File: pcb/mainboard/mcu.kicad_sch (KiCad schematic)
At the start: 54 parts, among them Y100 24MHz, Y101 32.768K

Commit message: Working on mainboard schematics
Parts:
- removed C137, C138: 18pF, Capacitor_SMD:C_0402_1005Metric, symbol Device:C
- removed Y101: 32.768K, Crystal:Crystal_SMD_TXC_9HT11-2Pin_2.0x1.2mm_HandSoldering, symbol Device:Crystal
- added R?: 100K/1%, Resistor_SMD:R_0402_1005Metric, symbol Device:R
- added R?: 10K, Resistor_SMD:R_0402_1005Metric, symbol Device:R
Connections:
- net GND: now also R?.1, R?.1
- net RTC_0P8: now also U?.B25 (RTC_XTALO)
- net PMIC_ON_REQ: now reaches U?.A24 (PMIC_ON_REQ)
- net CLK_32K_OUT: now reaches U?.A26 (RTC_XTALI)
- net POR_B: now reaches U?.B24 (POR_B)
- net at U?.D27 (JTAG_MOD): now also R?.2
- net PMIC_STBY_REQ: now reaches U?.E24 (PMIC_STBY_REQ)
- net RTC_RESET_B: now reaches U?.F24 (RTC_RESET_B)
- net at U?.J24 (TSENSOR_RES_EXT): now also R?.2
- no-connect marks 12 -> 17
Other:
- moved on the sheet: C123, C124, U?L, Y100

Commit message: Mainboard schematics WIP
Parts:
- gave numbers to parts that had none: 48
- renumbered C123 to C218, C124 to C224, Y100 to Y201

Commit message: Draft motherboard schematics for r0.0 layout
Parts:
- added R203: 100K, Resistor_SMD:R_0402_1005Metric, symbol Device:R
- added R204, R205, R206, R207: 10K, Resistor_SMD:R_0402_1005Metric, symbol Device:R
- added SW201: SW_Push, Button_Switch_SMD:SW_SPST_SKQG_WithStem, symbol Switch:SW_Push
- C202, C203: footprint Capacitor_SMD:C_0402_1005Metric -> Capacitor_SMD:C_0201_0603Metric
- R202: value 100K/1% -> 100K/1%
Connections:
- net GND: now also R204.1, R207.1, SW201.2
- net RTC_1P8: now also R203.2, R205.1, R206.1
- net ONOFF: now reaches U201.A25 (ONOFF)
- net ONOFF: now also R203.1
- net at U201.C27 (BOOT_MODE2): now also R206.2, SW201.1
- net at U201.D26 (BOOT_MODE3): now also R207.2
- net at U201.G26 (BOOT_MODE0): now also R204.2
- net at U201.G27 (BOOT_MODE1): now also R205.2
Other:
- note added: "QSPI boot by default, press button changes to eMMC boot (invalid) so it should fallback to USB"

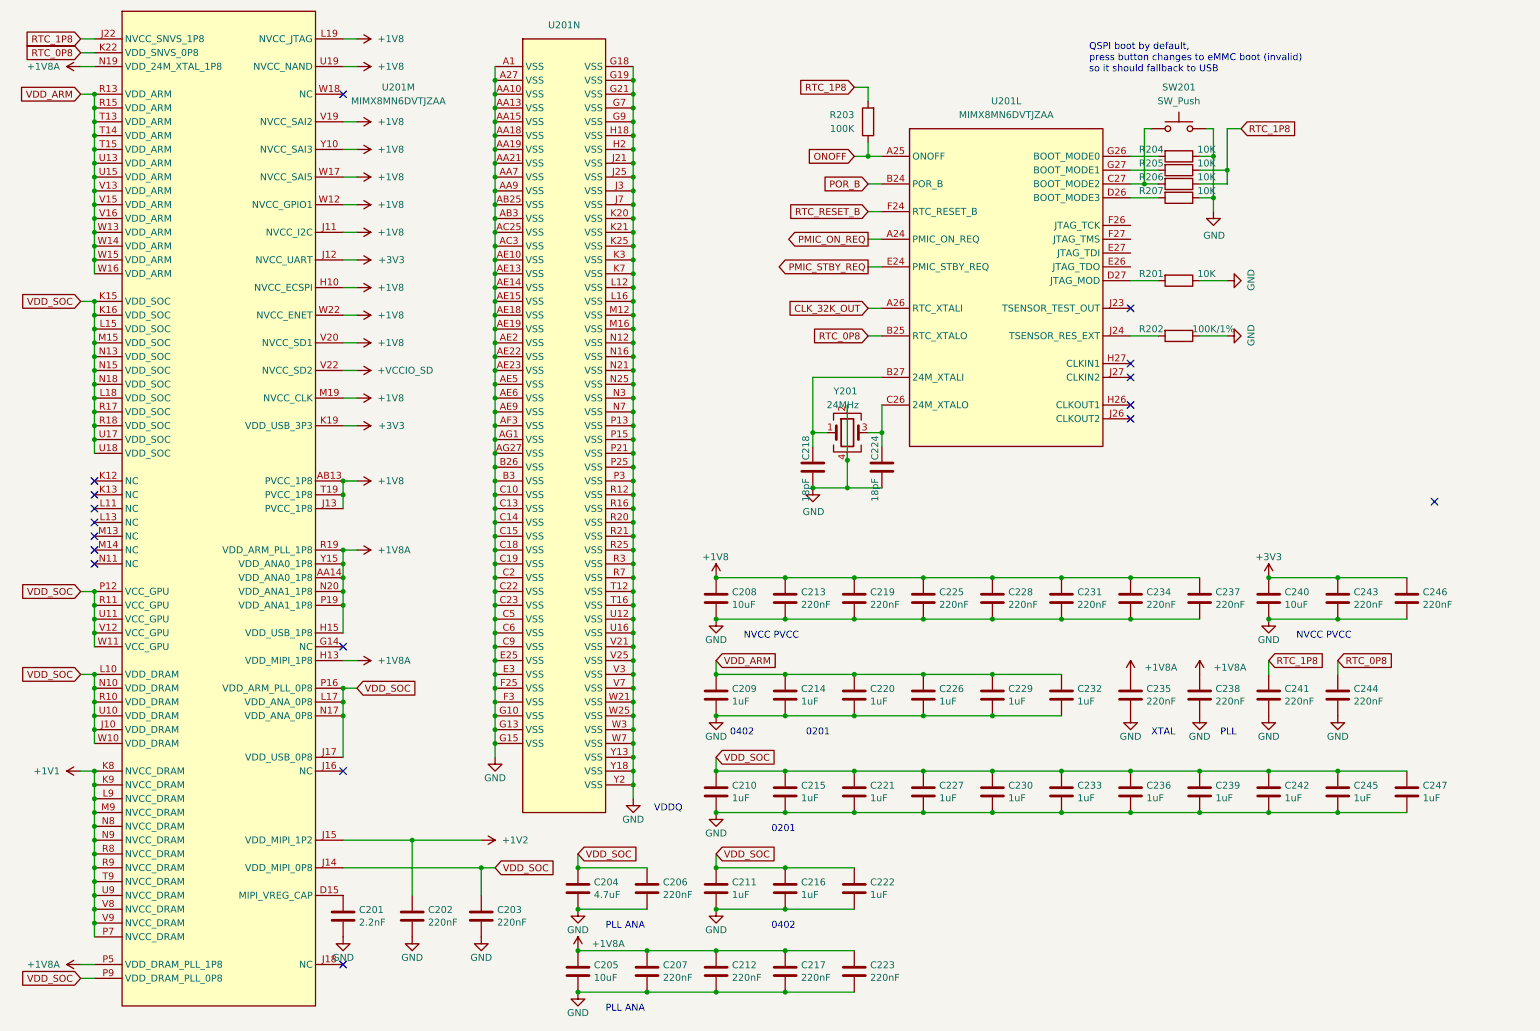
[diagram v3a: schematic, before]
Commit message: Motherboard PCB component initial placement, schematics fixes
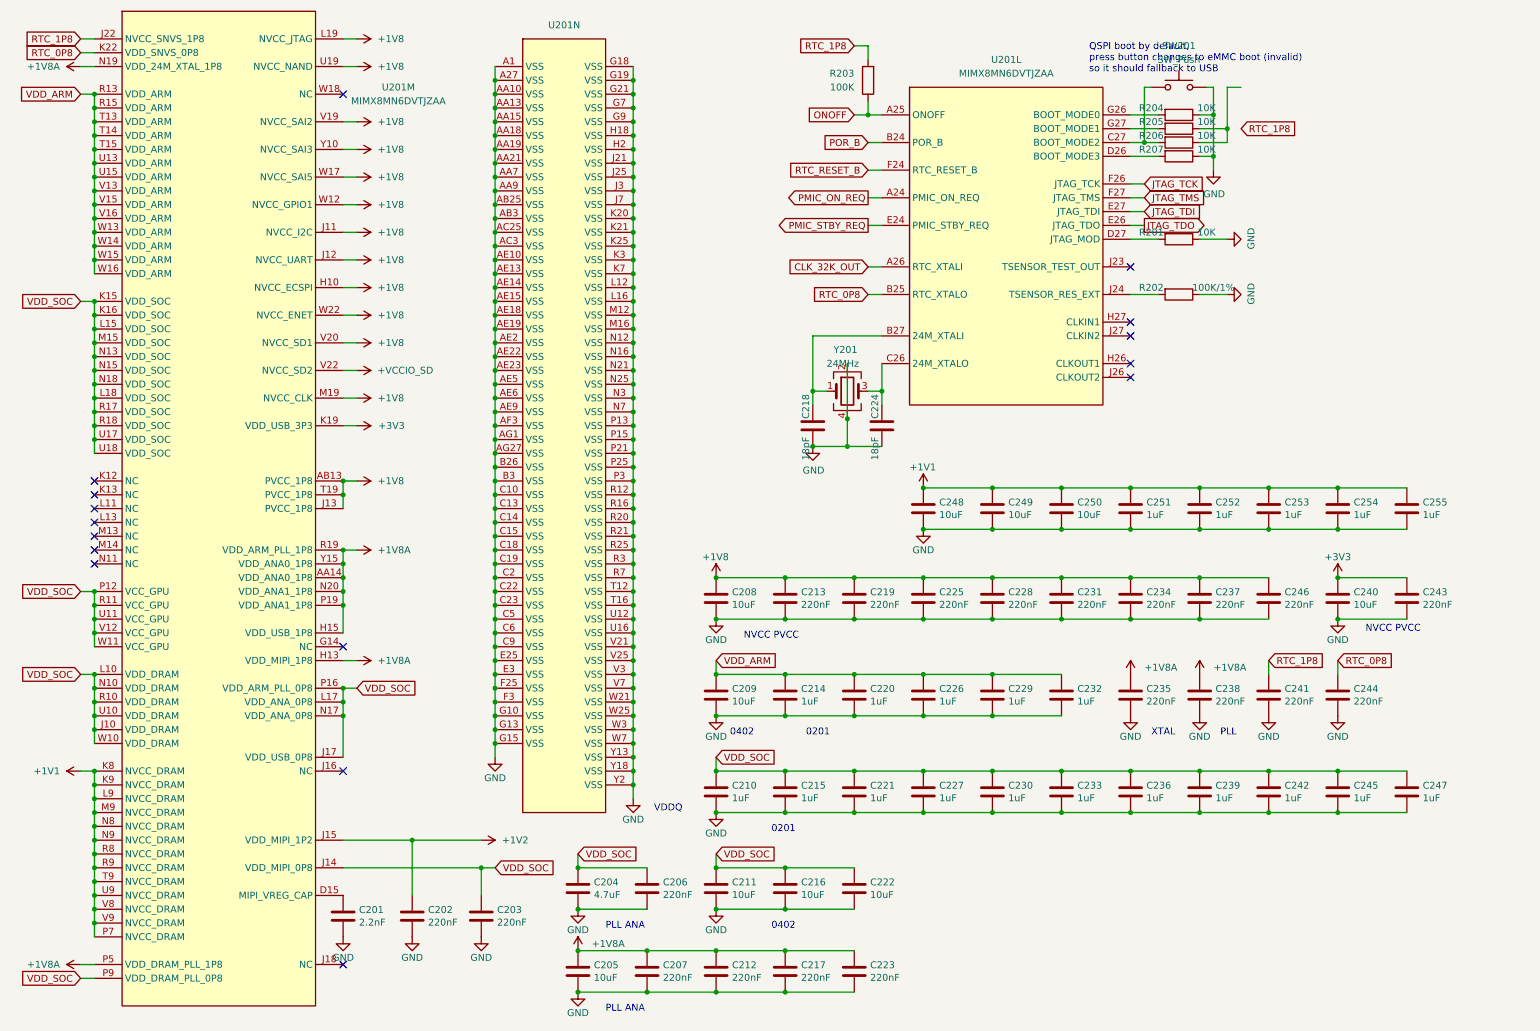
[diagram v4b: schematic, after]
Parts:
- added C248, C249, C250: 10uF, Capacitor_SMD:C_0402_1005Metric, symbol Device:C
- added C251, C252, C253, C254, C255: 1uF, Capacitor_SMD:C_0201_0603Metric, symbol Device:C
- C209, C211, C216, C222: value 1uF -> 10uF
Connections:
- net +1V1: now also C248.1, C249.1, C250.1, C251.1, C252.1, C253.1, C254.1, C255.1
- net +1V8: now also C246.1, U201.J12 (NVCC_UART)
- net +3V3: no longer C246.1, U201.J12 (NVCC_UART)
- net GND: now also C248.2, C249.2, C250.2, C251.2, C252.2, C253.2, C254.2, C255.2
- net RTC_1P8: no longer R205.1, R206.1
- net JTAG_TDO: now reaches U201.E26 (JTAG_TDO)
- net JTAG_TDI: now reaches U201.E27 (JTAG_TDI)
- net JTAG_TCK: now reaches U201.F26 (JTAG_TCK)
- net JTAG_TMS: now reaches U201.F27 (JTAG_TMS)
- new net: R205.1, R206.1
- no-connect marks 17 -> 16
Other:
- moved on the sheet: C218, C224, C240, C243, C246, R201, R202, R203, R204, R205, R206, R207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

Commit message: Routing mainboard in progress, schematics fixes
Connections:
- net RTC_1P8: now also R205.1, R206.1
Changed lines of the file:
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@@
   )
   (text "QSPI boot by default,\npress button changes to eMMC boot (invalid)\nso it should fallback to USB"
-    (at 210.82 25.4 0)
+    (at 238.76 38.1 0)
     (effects (font (size 1.27 1.27)) (justify left bottom))
   )
@@
     )
   )
-  (global_label "RTC_1P8" (shape input) (at 238.76 35.56 0) (fields_autoplaced)
+  (global_label "RTC_1P8" (shape input) (at 238.76 27.94 0) (fields_autoplaced)
     (effects (font (size 1.27 1.27)) (justify left))
-    (property "Intersheet References" "${INTERSHEET_REFS}" (id 0) (at 249.5279 35.6394 0)
+    (property "Intersheet References" "${INTERSHEET_REFS}" (id 0) (at 249.5279 28.0194 0)
       (effects (font (size 1.27 1.27)) (justify left) hide)
     )

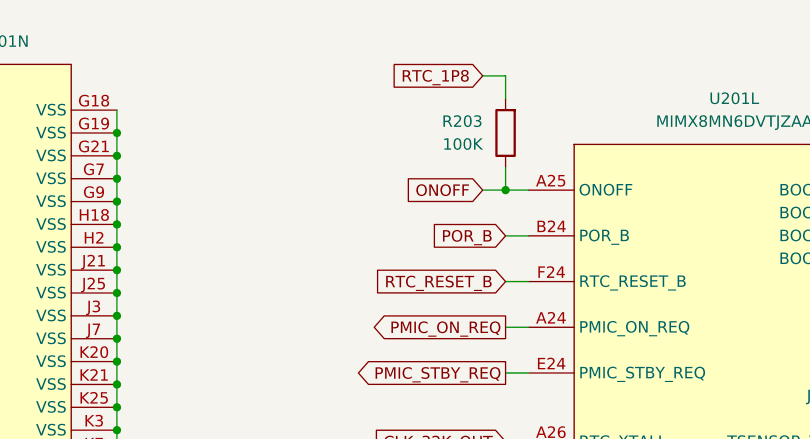
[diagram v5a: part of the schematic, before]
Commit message: Mainboard design bug fixes
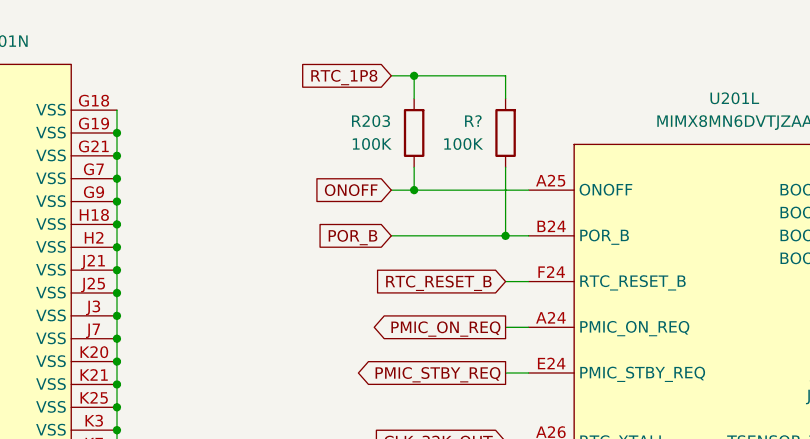
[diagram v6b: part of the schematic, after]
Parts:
- added R?: 100K, Resistor_SMD:R_0402_1005Metric, symbol Device:R
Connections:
- net POR_B: now also R?.1
- net RTC_1P8: now also R?.2
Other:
- moved on the sheet: R203
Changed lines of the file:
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@@
   (junction (at 154.94 118.11) (diameter 0) (color 0 0 0 0)
   )
+  (junction (at 160.02 33.02) (diameter 0) (color 0 0 0 0)
+  )
   (junction (at 127 105.41) (diameter 0) (color 0 0 0 0)
   )
@@
   (junction (at 218.44 125.73) (diameter 0) (color 0 0 0 0)
   )
+  (junction (at 170.18 38.1) (diameter 0) (color 0 0 0 0)
+  )
   (junction (at 193.04 101.6) (diameter 0) (color 0 0 0 0)
   )
@@
   (junction (at 127 151.13) (diameter 0) (color 0 0 0 0)
   )
-  (junction (at 170.18 33.02) (diameter 0) (color 0 0 0 0)
-  )
   (junction (at 27.94 46.99) (diameter 0) (color 0 0 0 0)
   )
@@
   (junction (at 101.6 148.59) (diameter 0) (color 0 0 0 0)
   )
+  (junction (at 160.02 20.32) (diameter 0) (color 0 0 0 0)
+  )
   (junction (at 101.6 82.55) (diameter 0) (color 0 0 0 0)
   )
@@
     (stroke (width 0) (type default) (color 0 0 0 0))
   )
+  (wire (pts (xy 170.18 30.48) (xy 170.18 38.1))
+    (stroke (width 0) (type default) (color 0 0 0 0))
+  )
   (wire (pts (xy 172.72 93.98) (xy 166.37 93.98))
     (stroke (width 0) (type solid) (color 0 0 0 0))
   )
+  (wire (pts (xy 160.02 33.02) (xy 172.72 33.02))
+    (stroke (width 0) (type default) (color 0 0 0 0))
+  )
   (wire (pts (xy 167.64 143.51) (xy 180.34 143.51))
     (stroke (width 0) (type default) (color 0 0 0 0))
@@
     (stroke (width 0) (type default) (color 0 0 0 0))
   )
-  (wire (pts (xy 170.18 38.1) (xy 172.72 38.1))
+  (wire (pts (xy 157.48 38.1) (xy 170.18 38.1))
     (stroke (width 0) (type default) (color 0 0 0 0))
   )
@@
     (stroke (width 0) (type default) (color 0 0 0 0))
   )
+  (wire (pts (xy 170.18 20.32) (xy 170.18 22.86))
+    (stroke (width 0) (type default) (color 0 0 0 0))
+  )
   (wire (pts (xy 101.6 57.15) (xy 101.6 59.69))
     (stroke (width 0) (type default) (color 0 0 0 0))
@@
     (stroke (width 0) (type default) (color 0 0 0 0))
   )
+  (wire (pts (xy 157.48 33.02) (xy 160.02 33.02))
+    (stroke (width 0) (type default) (color 0 0 0 0))
+  )
   (wire (pts (xy 180.34 118.11) (xy 193.04 118.11))
     (stroke (width 0) (type default) (color 0 0 0 0))
@@
     (stroke (width 0) (type default) (color 0 0 0 0))
   )
+  (wire (pts (xy 160.02 20.32) (xy 170.18 20.32))
+    (stroke (width 0) (type default) (color 0 0 0 0))
+  )
   (wire (pts (xy 116.84 194.31) (xy 129.54 194.31))
     (stroke (width 0) (type default) (color 0 0 0 0))
@@
     (stroke (width 0) (type default) (color 0 0 0 0))
   )
+  (wire (pts (xy 170.18 38.1) (xy 172.72 38.1))
+    (stroke (width 0) (type default) (color 0 0 0 0))
+  )
   (wire (pts (xy 180.34 153.67) (xy 193.04 153.67))
     (stroke (width 0) (type default) (color 0 0 0 0))
@@
     (stroke (width 0) (type default) (color 0 0 0 0))
   )
-  (wire (pts (xy 170.18 20.32) (xy 170.18 22.86))
+  (wire (pts (xy 160.02 20.32) (xy 160.02 22.86))
     (stroke (width 0) (type default) (color 0 0 0 0))
   )
@@
     (stroke (width 0) (type default) (color 0 0 0 0))
   )
-  (wire (pts (xy 170.18 30.48) (xy 170.18 33.02))
+  (wire (pts (xy 160.02 30.48) (xy 160.02 33.02))
     (stroke (width 0) (type default) (color 0 0 0 0))
   )
@@
     (stroke (width 0) (type default) (color 0 0 0 0))
   )
-  (wire (pts (xy 170.18 33.02) (xy 172.72 33.02))
-    (stroke (width 0) (type default) (color 0 0 0 0))
-  )
   (wire (pts (xy 170.18 43.18) (xy 172.72 43.18))
     (stroke (width 0) (type default) (color 0 0 0 0))
@@
     (stroke (width 0) (type default) (color 0 0 0 0))
   )
-  (wire (pts (xy 167.64 33.02) (xy 170.18 33.02))
-    (stroke (width 0) (type default) (color 0 0 0 0))
-  )
   (wire (pts (xy 193.04 161.29) (xy 205.74 161.29))
     (stroke (width 0) (type default) (color 0 0 0 0))
@@
     (stroke (width 0) (type default) (color 0 0 0 0))
   )
-  (wire (pts (xy 167.64 20.32) (xy 170.18 20.32))
+  (wire (pts (xy 157.48 20.32) (xy 160.02 20.32))
     (stroke (width 0) (type default) (color 0 0 0 0))
   )
@@
     )
   )
-  (global_label "ONOFF" (shape input) (at 167.64 33.02 180) (fields_autoplaced)
+  (global_label "ONOFF" (shape input) (at 157.48 33.02 180) (fields_autoplaced)
     (effects (font (size 1.27 1.27)) (justify right))
-    (property "Intersheet References" "${INTERSHEET_REFS}" (id 0) (at 158.8678 32.9406 0)
+    (property "Intersheet References" "${INTERSHEET_REFS}" (id 0) (at 148.7078 32.9406 0)
       (effects (font (size 1.27 1.27)) (justify right) hide)
     )
@@
     )
   )
-  (global_label "POR_B" (shape input) (at 170.18 38.1 180) (fields_autoplaced)
+  (global_label "POR_B" (shape input) (at 157.48 38.1 180) (fields_autoplaced)
     (effects (font (size 1.27 1.27)) (justify right))
-    (property "Intersheet References" "${INTERSHEET_REFS}" (id 0) (at 161.4683 38.0206 0)
+    (property "Intersheet References" "${INTERSHEET_REFS}" (id 0) (at 148.7683 38.0206 0)
       (effects (font (size 1.27 1.27)) (justify right) hide)
     )
@@
     )
   )
-  (global_label "RTC_1P8" (shape input) (at 167.64 20.32 180) (fields_autoplaced)
+  (global_label "RTC_1P8" (shape input) (at 157.48 20.32 180) (fields_autoplaced)
     (effects (font (size 1.27 1.27)) (justify right))
-    (property "Intersheet References" "${INTERSHEET_REFS}" (id 0) (at 156.8721 20.2406 0)
+    (property "Intersheet References" "${INTERSHEET_REFS}" (id 0) (at 146.7121 20.2406 0)
       (effects (font (size 1.27 1.27)) (justify right) hide)
     )
@@
     (pin "2")
   )
+  (symbol (lib_id "Device:R") (at 170.18 26.67 180) (unit 1)
+    (in_bom yes) (on_board yes)
+    (property "Reference" "R?" (id 0) (at 167.64 25.4 0)
+      (effects (font (size 1.27 1.27)) (justify left))
+    )
+    (property "Value" "100K" (id 1) (at 167.64 27.94 0)
+      (effects (font (size 1.27 1.27)) (justify left))
+    )
+    (property "Footprint" "Resistor_SMD:R_0402_1005Metric" (id 2) (at 171.958 26.67 90)
+      (effects (font (size 1.27 1.27)) hide)
+    )
+    (property "Datasheet" "~" (id 3) (at 170.18 26.67 0)
+      (effects (font (size 1.27 1.27)) hide)
+    )
+    (property "LCSC" "C93929" (id 4) (at 170.18 26.67 0)
+      (effects (font (size 1.27 1.27)) hide)
+    )
+    (property "Ref.Price" "0.002" (id 5) (at 170.18 26.67 0)
+      (effects (font (size 1.27 1.27)) hide)
+    )
+    (pin "1")
+    (pin "2")
+  )
   (symbol (lib_id "Device:C") (at 154.94 175.26 0) (unit 1)
     (in_bom yes) (on_board yes)
@@
     (pin "1")
   )
-  (symbol (lib_id "Device:R") (at 170.18 26.67 180) (unit 1)
+  (symbol (lib_id "Device:R") (at 160.02 26.67 180) (unit 1)
     (in_bom yes) (on_board yes)
-    (property "Reference" "R203" (id 0) (at 167.64 25.4 0)
+    (property "Reference" "R203" (id 0) (at 157.48 25.4 0)
       (effects (font (size 1.27 1.27)) (justify left))
     )
-    (property "Value" "100K" (id 1) (at 167.64 27.94 0)
+    (property "Value" "100K" (id 1) (at 157.48 27.94 0)
       (effects (font (size 1.27 1.27)) (justify left))
     )
-    (property "Footprint" "Resistor_SMD:R_0402_1005Metric" (id 2) (at 171.958 26.67 90)
+    (property "Footprint" "Resistor_SMD:R_0402_1005Metric" (id 2) (at 161.798 26.67 90)
       (effects (font (size 1.27 1.27)) hide)
     )
-    (property "Datasheet" "~" (id 3) (at 170.18 26.67 0)
+    (property "Datasheet" "~" (id 3) (at 160.02 26.67 0)
       (effects (font (size 1.27 1.27)) hide)
     )
-    (property "LCSC" "C93929" (id 4) (at 170.18 26.67 0)
+    (property "LCSC" "C93929" (id 4) (at 160.02 26.67 0)
       (effects (font (size 1.27 1.27)) hide)
     )
-    (property "Ref.Price" "0.002" (id 5) (at 170.18 26.67 0)
+    (property "Ref.Price" "0.002" (id 5) (at 160.02 26.67 0)
       (effects (font (size 1.27 1.27)) hide)
     )

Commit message: Keypad bugfix, pulling in submodules
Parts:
- gave numbers to parts that had none: 1
